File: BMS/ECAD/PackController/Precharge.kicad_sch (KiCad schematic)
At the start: 38 parts, among them K1101 KT12-1A-40L-THT, Q1101 DMP4065S-7, Q1102 IXTA08N100D2HV, Q1103 BC846, Q1104 IRLML0100TR, U1101 TCLT1004, U1102 TCLT1004, U1103 TEA1-0505HI, U1104 SN74LVC2G14DBV

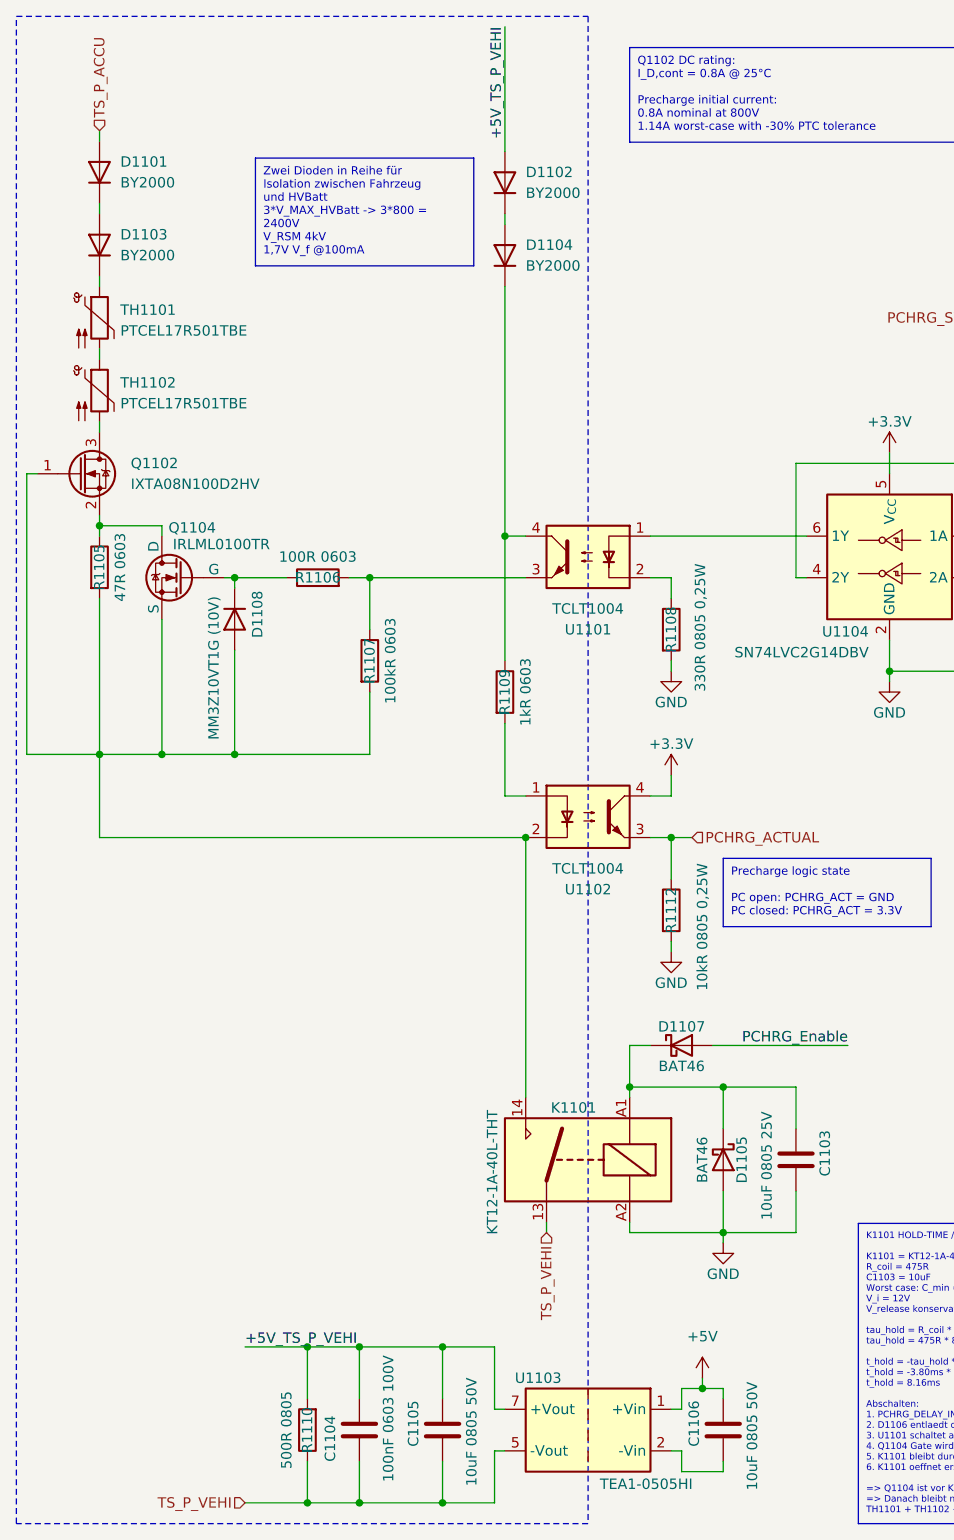
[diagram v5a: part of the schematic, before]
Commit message: add rule areas for hv separation
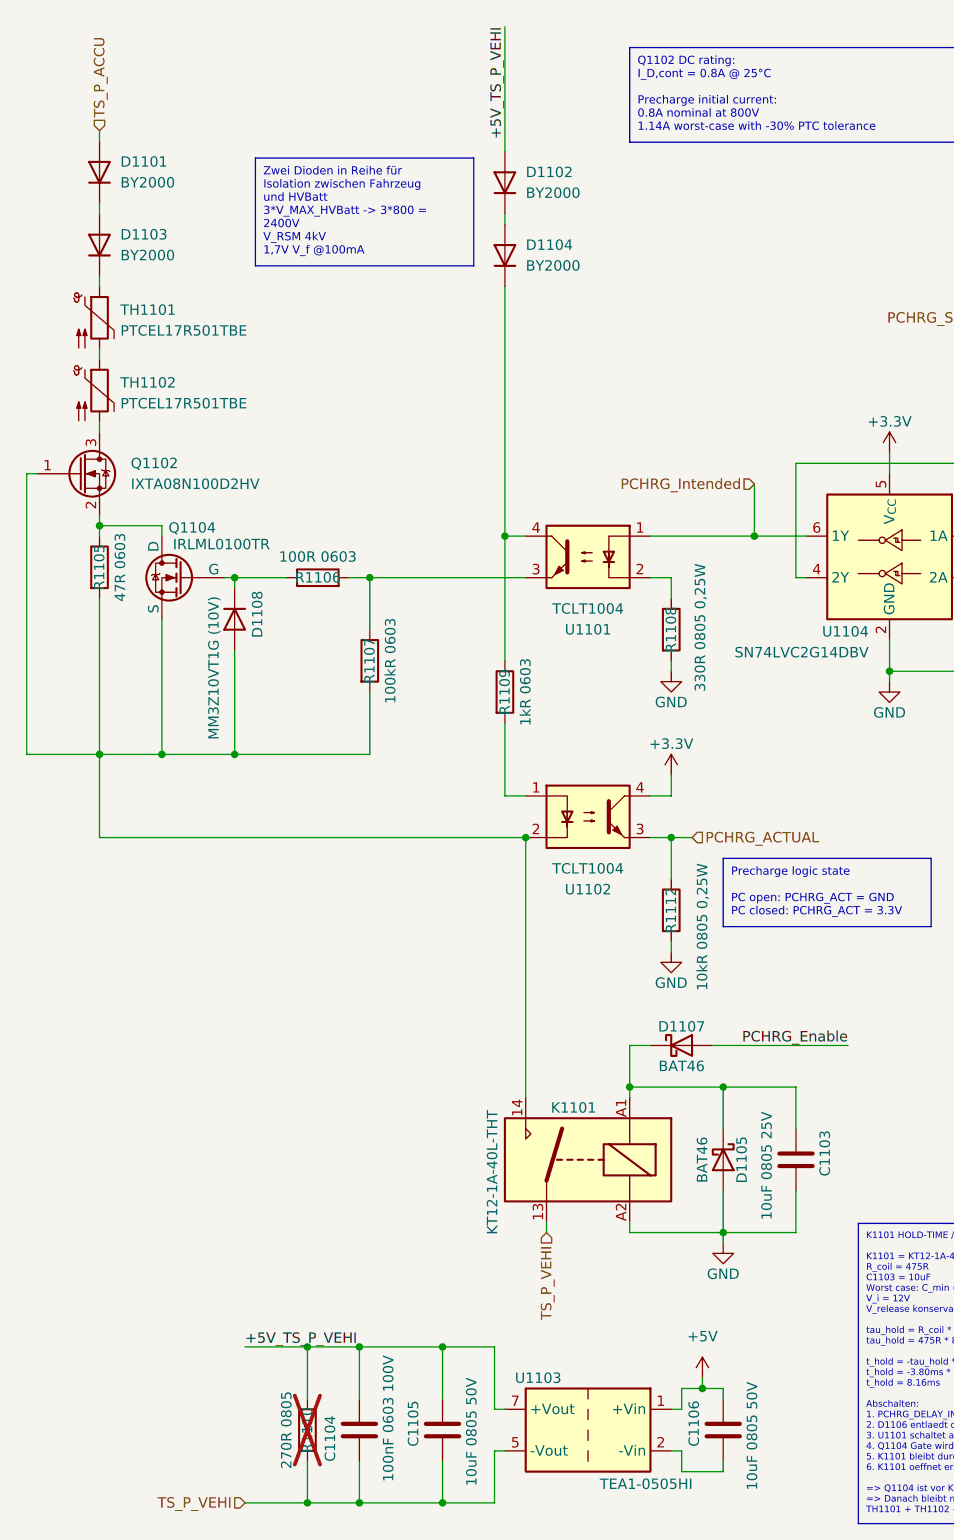
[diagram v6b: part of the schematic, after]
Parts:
- R1110: value 500R 0805 -> 270R 0805; now not fitted
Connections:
- net PCHRG_Intended: now reaches U1101.1, U1104.6 (1Y)

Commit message: route HV components
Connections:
- net GND: now also C1106.2, U1103.2 (-Vin)
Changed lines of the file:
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@@
 	)
 	(junction
+		(at 100.33 190.5)
+		(diameter 0)
+		(color 0 0 0 0)
+	)
+	(junction
 		(at 147.32 92.71)
 		(diameter 0)
@@
 		(polyline
 			(pts
-				(xy 13.335 12.7) (xy 83.7406 13.335) (xy 83.8994 197.485) (xy 13.4938 196.85)
+				(xy 13.335 12.7) (xy 83.82 12.7) (xy 83.8994 197.485) (xy 13.4938 196.85)
 			)
 			(stroke
@@
 		(length 2.54)
 		(shape round)
-		(at 15.24 12.7 180)
+		(at 34.29 12.7 180)
 		(fields_autoplaced yes)
 		(effects
@@
 		)
 		(property "Netzklasse" "HV800"
-			(at 15.9385 15.24 0)
+			(at 34.9885 15.24 0)
 			(show_name no)
 			(do_not_autoplace no)
@@
 		)
 		(property "Component Class" ""
-			(at -7.62 -66.04 0)
+			(at 11.43 -66.04 0)
 			(show_name no)
 			(do_not_autoplace no)
@@
 					(unit 1)
 				)
+			)
+		)
+	)
+	(symbol
+		(lib_id "power:GND")
+		(at 100.33 190.5 0)
+		(unit 1)
+		(body_style 1)
+		(exclude_from_sim no)
+		(in_bom yes)
+		(on_board yes)
+		(in_pos_files yes)
+		(dnp no)
+		(property "Reference" "#PWR01104"
+			(at 100.33 196.85 0)
+			(hide yes)
+			(show_name no)
+			(do_not_autoplace no)
+			(effects
+				(font
+					(size 1.27 1.27)
+				)
+			)
+		)
+		(property "Value" "GND"
+			(at 100.33 194.31 0)
+			(show_name no)
+			(do_not_autoplace no)
+			(effects
+				(font
+					(size 1.27 1.27)
+				)
+			)
+		)
+		(property "Footprint" ""
+			(at 100.33 190.5 0)
+			(hide yes)
+			(show_name no)
+			(do_not_autoplace no)
+			(effects
+				(font
+					(size 1.27 1.27)
+				)
+			)
+		)
+		(property "Datasheet" ""
+			(at 100.33 190.5 0)
+			(hide yes)
+			(show_name no)
+			(do_not_autoplace no)
+			(effects
+				(font
+					(size 1.27 1.27)
+				)
+			)
+		)
+		(property "Description" ""
+			(at 100.33 190.5 0)
+			(show_name no)
+			(do_not_autoplace no)
+			(effects
+				(font
+					(size 1.27 1.27)
+				)
+			)
+		)
+		(pin "1"
+		)
+		(instances
+			(project "Pack_Controller"
+				(path "/58a1c93e-baba-4d23-9191-955e00968735/10db8ab2-a069-4c18-98c6-f1c7e2899a80"
+					(reference "#PWR01104")
+					(unit 1)
+				)
